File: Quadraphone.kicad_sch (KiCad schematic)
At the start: 37 parts, among them J1 Conn_01x10_Male, J2 Conn_01x10_Male, J3 Conn_01x10_Male, J4 Conn_01x10_Male, J5 Eurorack_10_pin_power, U1 AMS1117-5.0, U14 LM4040DBZ-2.5, U3 MCP6002, U4 LM4040DBZ-5, U5 MCP6004, U8 4066

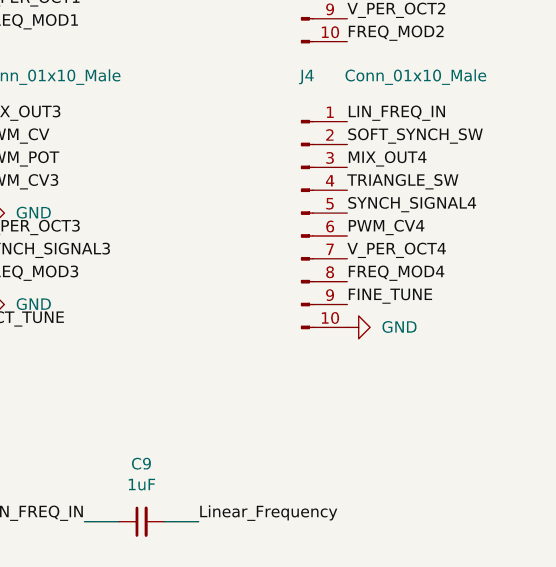
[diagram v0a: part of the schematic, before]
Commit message: Started laying out control board
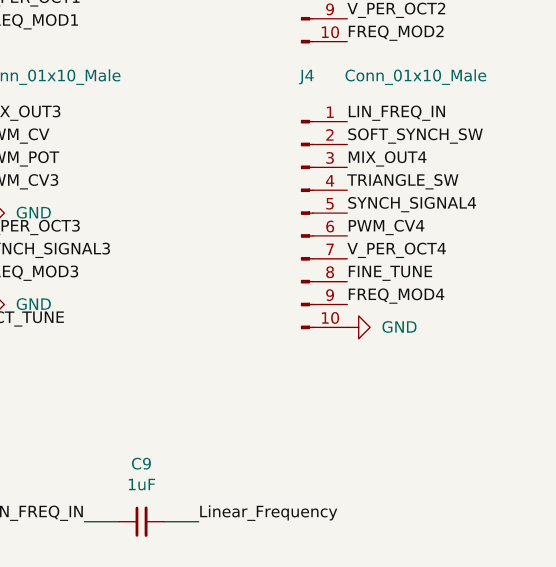
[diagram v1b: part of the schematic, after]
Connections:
- net FINE_TUNE: now also J4.8 (Pin_8); no longer J4.9 (Pin_9)
- net FREQ_MOD4: now also J4.9 (Pin_9); no longer J4.8 (Pin_8)
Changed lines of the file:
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@@
     (effects (font (size 1.27 1.27)) (justify left bottom))
   )
-  (label "FREQ_MOD4" (at 252.73 76.2 0)
+  (label "FREQ_MOD4" (at 252.73 78.74 0)
     (effects (font (size 1.27 1.27)) (justify left bottom))
   )
@@
     (effects (font (size 1.27 1.27)) (justify right bottom))
   )
-  (label "FINE_TUNE" (at 252.73 78.74 0)
+  (label "FINE_TUNE" (at 252.73 76.2 0)
     (effects (font (size 1.27 1.27)) (justify left bottom))
   )

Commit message: Started laying out Panel
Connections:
- net FINE_TUNE: now also J3.10 (Pin_10); no longer J4.8 (Pin_8)
- net OCT_TUNE: now also J4.8 (Pin_8); no longer J3.10 (Pin_10)
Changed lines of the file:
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@@
     (effects (font (size 1.27 1.27)) (justify left bottom))
   )
-  (label "OCT_TUNE" (at 212.09 81.28 0)
+  (label "OCT_TUNE" (at 252.73 76.2 0)
     (effects (font (size 1.27 1.27)) (justify left bottom))
   )
@@
     (effects (font (size 1.27 1.27)) (justify right bottom))
   )
-  (label "FINE_TUNE" (at 252.73 76.2 0)
-    (effects (font (size 1.27 1.27)) (justify left bottom))
-  )
+  (label "FINE_TUNE" (at 212.09 81.28 0)
+    (effects (font (size 1.27 1.27)) (justify left bottom))
+  )

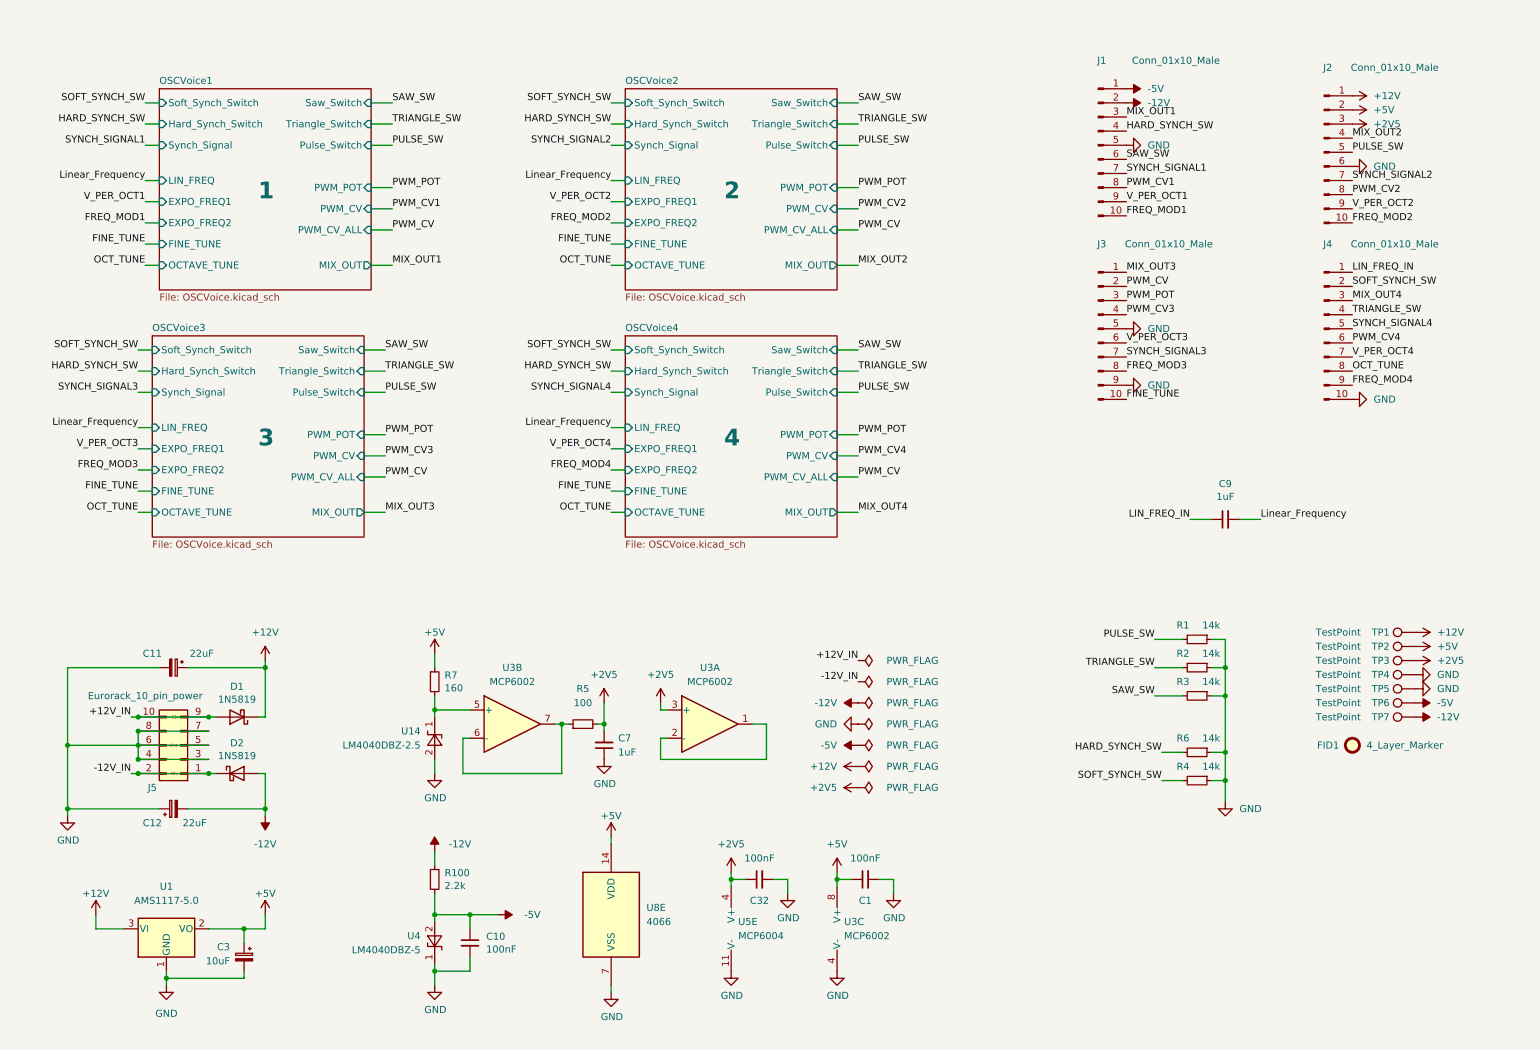
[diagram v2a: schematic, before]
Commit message: Fixed ground connections on component board
Added JLC PCB plug-in
Schematic clean-up
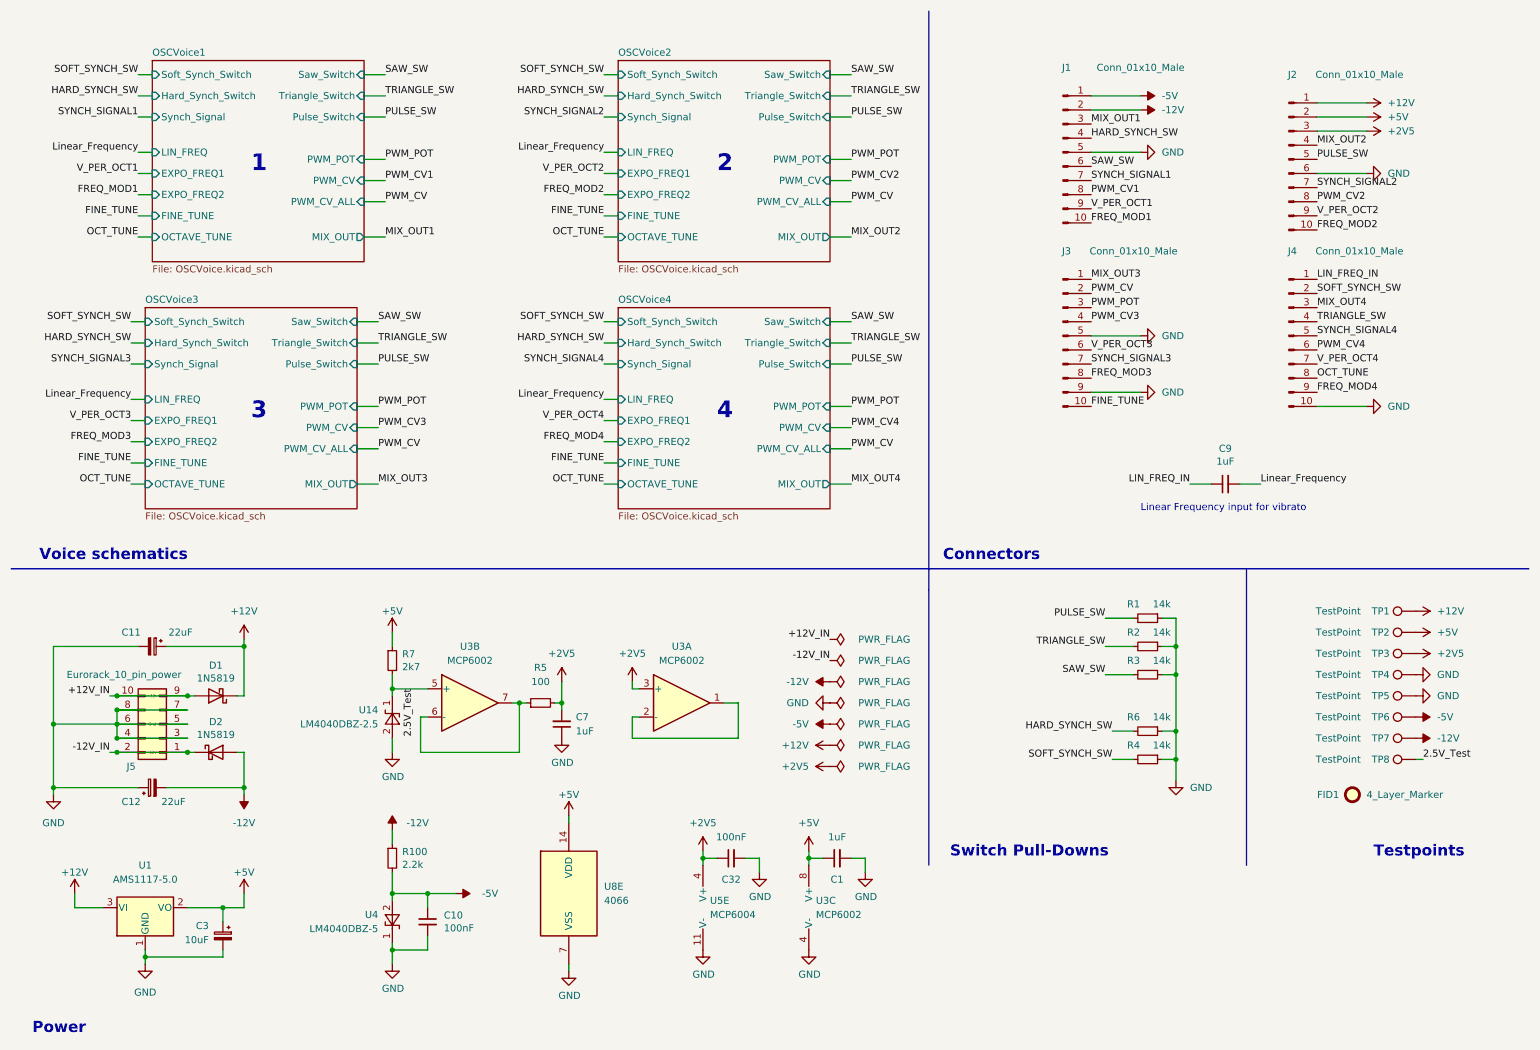
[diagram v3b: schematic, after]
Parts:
- added TP8: TestPoint, Custom_Footprints:1.3mm_Test_Point, symbol Connector:TestPoint
- C1: value 100nF -> 1uF
- R7: value 160 -> 2k7
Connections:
- net 2.5V_Test: now reaches R7.2, U14.1 (K), U3.5 (+)
- net 2.5V_Test: now also TP8.1
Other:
- note added: "Connectors"
- note added: "Linear Frequency input for vibrato"
- note added: "Power"
- note added: "Switch Pull-Downs"
- note added: "Testpoints"
- note added: "Voice schematics"
- company: (none) -> Mountjoy Modular
- title: (none) -> Quadraphone Components
- moved on the sheet: C1, C10, C11, C12, C3, C32, C7, C9, D1, D2, FID1, J1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

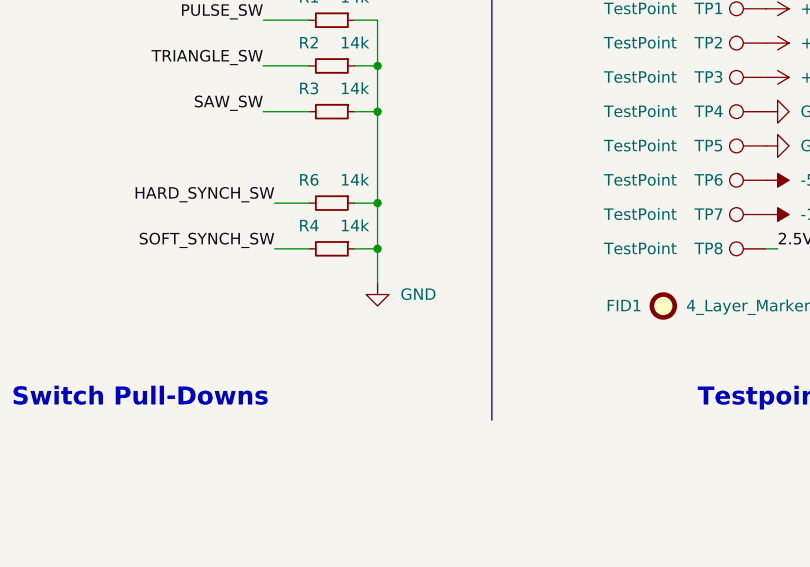
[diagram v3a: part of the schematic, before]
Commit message: Added RJ45 breakout module
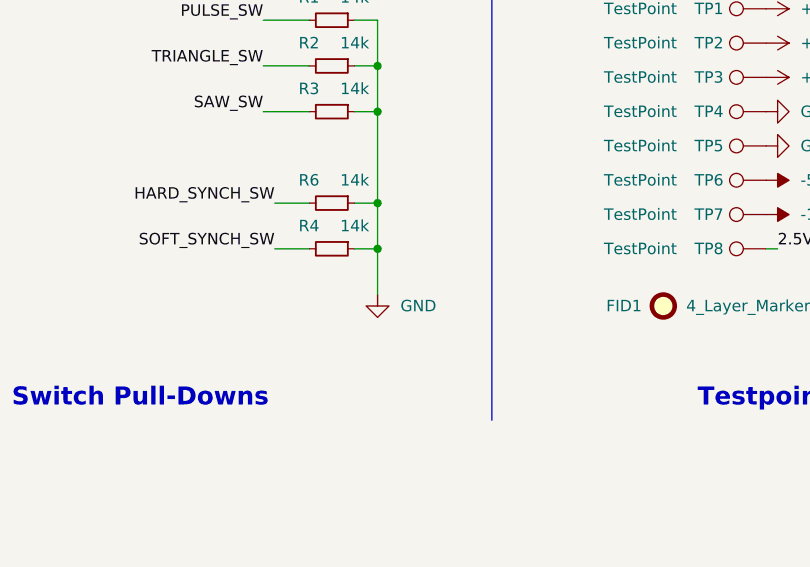
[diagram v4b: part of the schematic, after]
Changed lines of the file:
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@@
     (stroke (width 0) (type default) (color 0 0 0 0))
   )
-  (wire (pts (xy 220.98 146.05) (xy 220.98 149.86))
+  (wire (pts (xy 220.98 146.05) (xy 220.98 151.13))
     (stroke (width 0) (type default) (color 0 0 0 0))
   )
@@
     (pin "2")
   )
-  (symbol (lib_id "power:GND") (at 220.98 149.86 0) (unit 1)
-    (in_bom yes) (on_board yes) (fields_autoplaced)
-    (property "Reference" "#PWR0121" (id 0) (at 220.98 156.21 0)
-      (effects (font (size 1.27 1.27)) hide)
-    )
-    (property "Value" "GND" (id 1) (at 223.52 151.1299 0)
-      (effects (font (size 1.27 1.27)) (justify left))
-    )
-    (property "Footprint" "" (id 2) (at 220.98 149.86 0)
-      (effects (font (size 1.27 1.27)) hide)
-    )
-    (property "Datasheet" "" (id 3) (at 220.98 149.86 0)
-      (effects (font (size 1.27 1.27)) hide)
-    )
+  (symbol (lib_id "power:GND") (at 220.98 151.13 0) (unit 1)
+    (in_bom yes) (on_board yes) (fields_autoplaced)
+    (property "Reference" "#PWR0121" (id 0) (at 220.98 157.48 0)
+      (effects (font (size 1.27 1.27)) hide)
+    )
+    (property "Value" "GND" (id 1) (at 223.52 152.3999 0)
+      (effects (font (size 1.27 1.27)) (justify left))
+    )
+    (property "Footprint" "" (id 2) (at 220.98 151.13 0)
+      (effects (font (size 1.27 1.27)) hide)
+    )
+    (property "Datasheet" "" (id 3) (at 220.98 151.13 0)
+      (effects (font (size 1.27 1.27)) hide)
+    )

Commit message: Prepared all gerbers
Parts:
- R7: footprint Resistor_SMD:R_0603_1608Metric_Pad0.98x0.95mm_HandSolder -> Resistor_SMD:R_0603_1608Metric
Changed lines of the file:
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@@
       (effects (font (size 1.27 1.27)) (justify left))
     )
-    (property "Footprint" "Resistor_SMD:R_0603_1608Metric_Pad0.98x0.95mm_HandSolder" (id 2) (at 80.01 128.27 0)
+    (property "Footprint" "Resistor_SMD:R_0603_1608Metric" (id 2) (at 80.01 128.27 0)
       (effects (font (size 1.27 1.27)) hide)
     )
@@
     )
     (path "/d6a1ef48-3fb4-4411-8ea9-341924f44be8"
-      (reference "R7") (unit 1) (value "2k7") (footprint "Resistor_SMD:R_0603_1608Metric_Pad0.98x0.95mm_HandSolder")
+      (reference "R7") (unit 1) (value "2k7") (footprint "Resistor_SMD:R_0603_1608Metric")
     )
     (path "/07c473a3-19f8-4492-9997-b494b1996c87/60c24d85-a7f7-491a-9c0f-54e47fc539d5"
